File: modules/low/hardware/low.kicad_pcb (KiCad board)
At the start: 2 copper layers, 29 x 110 mm, 70 parts, among them J1 PJ301M-12, J10 Eurorack_2x5, J11 UPDI, J2 PJ301M-12, J3 PJ301M-12, J4 PJ301M-12, Q1 MMBT3904, U1 HT7533-1, U2 ATtiny1616-MNR, U3 MCP6002, U4 TS5A23157, U5 VTL5C, U6 MCP6002, U7 VTL5C, U8 MCP6002, U9 TL072

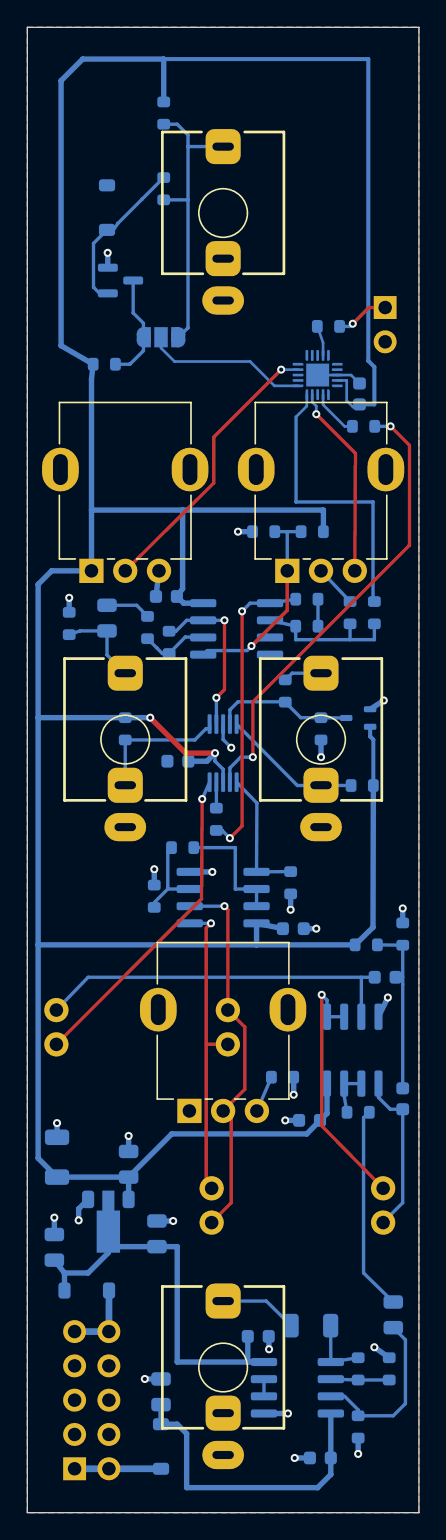
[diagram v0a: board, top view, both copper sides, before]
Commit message: LOW R2: 3 mm pot/jack clearance, edge pull-in, LCSC fields and JLCPCB export
- Move SMD parts >= 3 mm from pot/jack pads and away from side edges; re-route
- Add UPDI and JP1 back-silk labels
- Fix U6 pin 7 (LPG_AMP) link after the U6 move
- R17/R18 47k/100k (Basic) for the CV divider; LCSC/MPN fields on schematic and board
- JLCPCB export (bottom Economic PCBA) in modules/low/jlcpcb/

Co-Authored-By: Claude Opus 5.5 <noreply@anthropic.com>
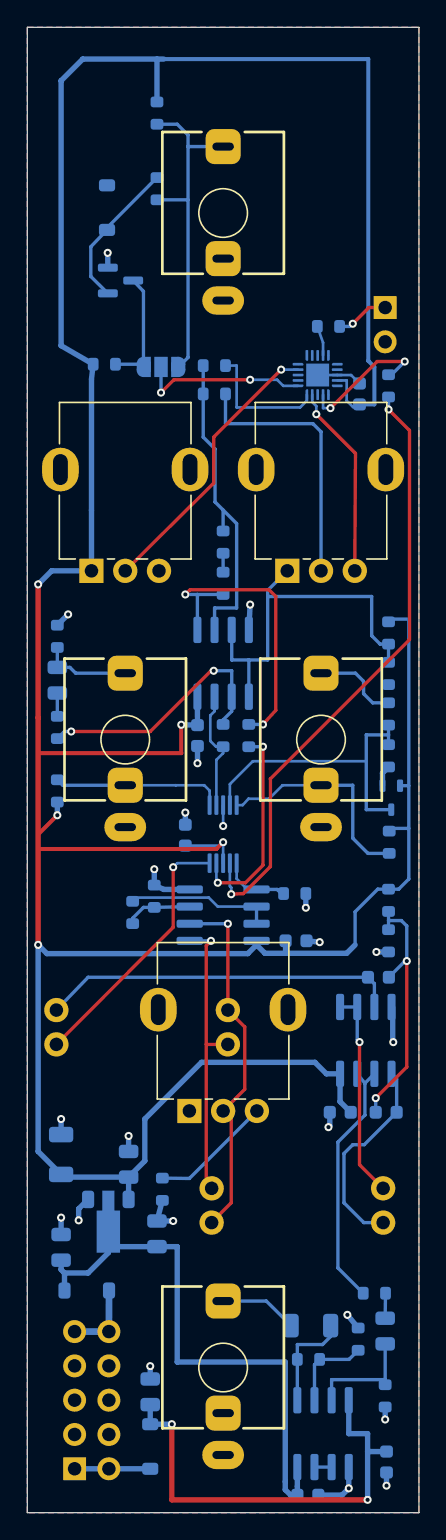
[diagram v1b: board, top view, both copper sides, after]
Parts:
- R17: value 51k -> 47k
- R18: value 110k -> 100k
- moved R5 21.8 mm to (114.3, 84.3), turned to 180 degrees
- moved R6 19.1 mm to (114.3, 86.4), turned to 180 degrees
- moved R11 14.0 mm to (127.2, 107.1), turned to -90 degrees
- moved R20 13.5 mm to (126.2, 153.0)
- moved C16 12.3 mm to (121.3, 167.9)
- moved R26 12.2 mm to (110.5, 145.3), turned to -90 degrees
- moved C7 10.6 mm to (113.1, 111.7), turned to -90 degrees
- moved R14 9.97 mm to (102.7, 111.1)
- moved R10 9.39 mm to (127.2, 104.1), turned to -90 degrees
- moved R7 8.79 mm to (115.0, 97.4), turned to -90 degrees
- moved R15 7.98 mm to (115.0, 111.7), turned to -90 degrees
- moved R17 7.84 mm to (127.2, 110.1)
- moved R16 6.82 mm to (102.7, 115.8), turned to 90 degrees
- moved R9 6.65 mm to (116.9, 111.7), turned to -90 degrees
- moved D4 6.39 mm to (127.5, 116.3), turned to -90 degrees
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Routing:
- net /MIX_W: track 3.13 -> 19.8 mm
- net /LPG_AMP: track 3.41 -> 19.0 mm
- net /AIN_SUM: track 5.10 -> 19.2 mm, vias 0 -> 2
- net /LPG_OUT: track 15.2 -> 1.85 mm
- net /MCO_OUT: track 1.92 -> 15.2 mm, vias 0 -> 2
- net /MCO_SUM: track 11.1 -> 23.8 mm
- net /CVIN_DIV: track 10.4 -> 22.8 mm
- net +12V_F: track 28.8 -> 40.9 mm
- net /TONE1: track 21.4 -> 9.78 mm
- net /VEL_CV: track 34.1 -> 45.8 mm
- net /VMID_MCO: track 17.0 -> 28.3 mm, vias 1 -> 0
- net -12V_F: track 23.2 -> 33.3 mm, vias 0 -> 2
- net +3V3: track 259.3 -> 268.1 mm, vias 2 -> 5
- net /DAC: track 3.59 -> 10.1 mm, vias 0 -> 2
- net /VMID_LPG: track 13.0 -> 19.4 mm, vias 0 -> 2
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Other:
- board text added: "LOW R2"
- board text added: "PROT RX DIR"
- board text added: "UPDI"
- board text removed: "LOW R1"
